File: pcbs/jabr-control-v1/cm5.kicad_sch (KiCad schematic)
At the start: 8 parts, among them SW201 SW_Push

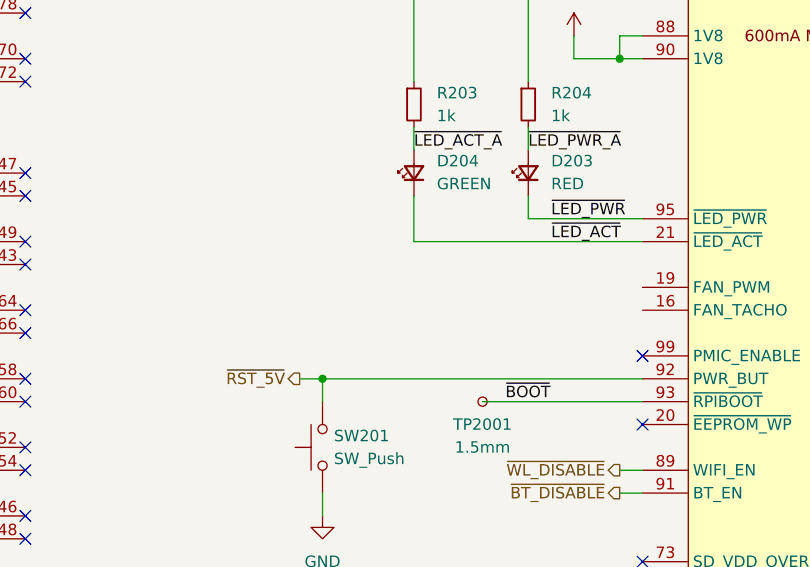
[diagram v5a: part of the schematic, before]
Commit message: Finished M.2 E-Key schematic
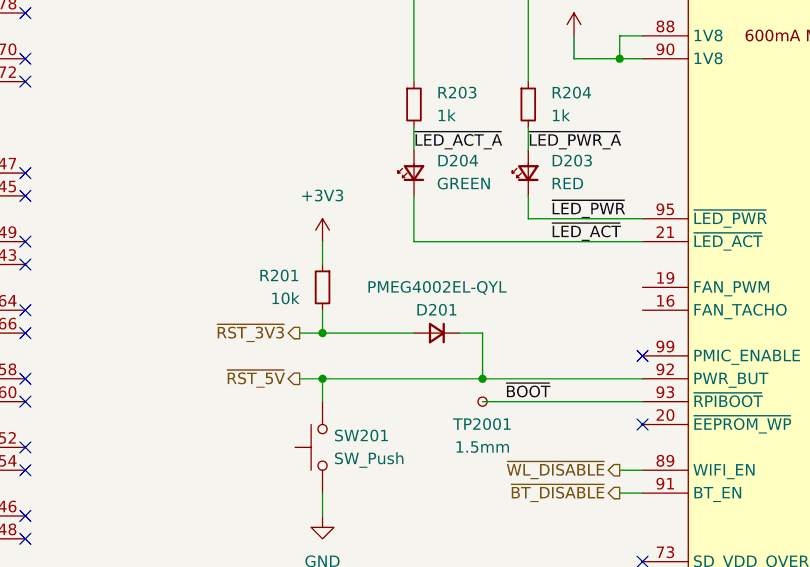
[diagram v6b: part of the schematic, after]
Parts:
- added D201: PMEG4002EL-QYL, project_footprints:PMEG4002EL-QYL, symbol DIODE:PMEG4002EL-QYL
- added R201: 10k, project_footprints:R_0402, symbol DEV:R_SMALL
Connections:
- net +3V3: now also R201.1
- net ~{RST_5V}: now also D201.1 (K)
- new net ~{RST_3V3}: D201.2 (A), R201.2

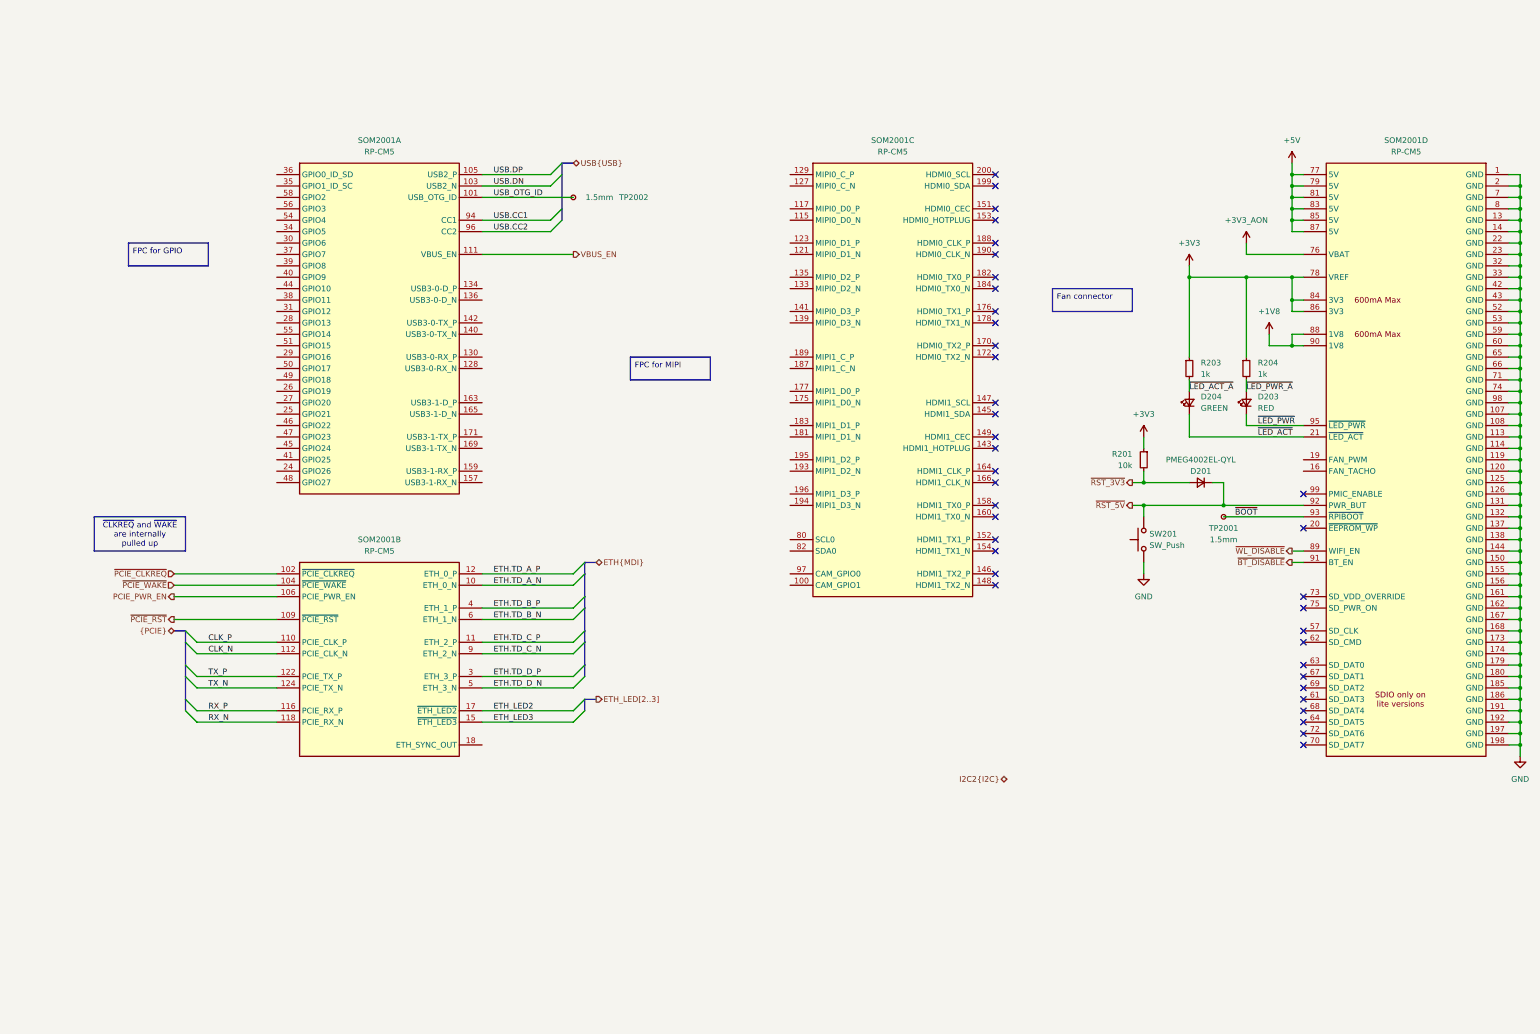
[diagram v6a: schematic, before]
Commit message: Schematic nearing completion, need to do GPIO and PHY decouplings caps
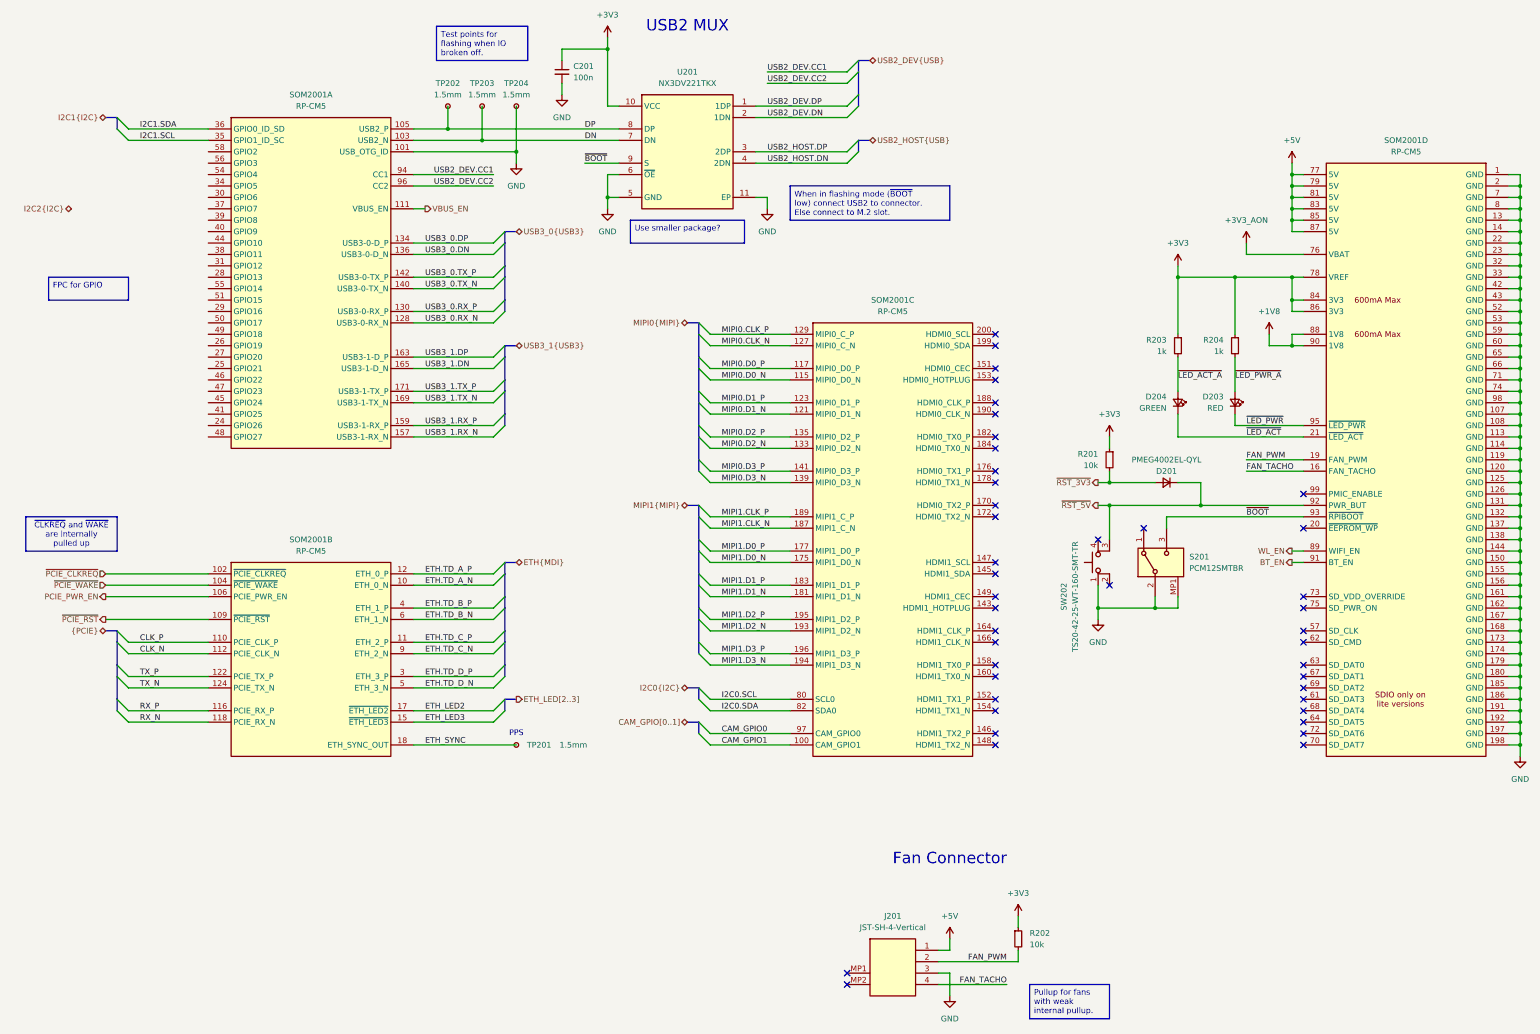
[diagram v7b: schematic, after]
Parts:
- removed SW201: SW_Push, symbol Switch:SW_Push
- removed TP2001, TP2002: 1.5mm, TestPoint:TestPoint_Pad_D1.5mm, symbol Connector:TestPoint_Small
- added C201: 100n, symbol DEV:C_SMALL
- added J201: JST-SH-4-Vertical, project_footprints:JST_SH_BM04B-SRSS-TB_1x04-1MP_P1.00mm_Vertical, symbol JST:JST-SH-4-Vertical
- added R202: 10k, project_footprints:R_0402, symbol DEV:R_SMALL
- added S201: PCM12SMTBR, project_footprints:PCM12SMTBR, symbol MECH:PCM12SMTBR
- added SW202: TS20-42-25-WT-160-SMT-TR, TS204225WT160SMTTR, symbol MECH:TS20-42-25-WT-160-SMT-TR
- added TP201, TP202, TP203, TP204: 1.5mm, project_footprints:TestPoint_Pad_D1.5mm, symbol Connector:TestPoint_Small
- added U201: NX3DV221TKX, project_footprints:SON50P300X300X100-11N, symbol COMM-MUX:NX3DV221TKX
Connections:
- net USB_OTG_ID is gone; now on net GND: SOM2001.101 (USB_OTG_ID)
- net +3V3: now also C201.1, R202.1, U201.10 (VCC)
- net +5V: now also J201.1
- net GND: now also C201.2, J201.3, S201.2 (COM), S201.MP1, S201.MP2, S201.MP3, S201.MP4, SW202.1, TP204.1, U201.11 (EP), U201.5 (GND), U201.6 (~{OE})
- net ~{BOOT}: now also S201.3 (NO), U201.9 (S)
- net ~{RST_5V}: now also SW202.3
- net ETH_SYNC: now reaches SOM2001.18 (ETH_SYNC_OUT)
- net ETH_SYNC: now also TP201.1
- net USB3_0.RX_N: now reaches SOM2001.128 (USB3-0-RX_N)
- net USB3_0.RX_P: now reaches SOM2001.130 (USB3-0-RX_P)
- net USB3_0.DP: now reaches SOM2001.134 (USB3-0-D_P)
- net USB3_0.DN: now reaches SOM2001.136 (USB3-0-D_N)
- net USB3_0.TX_N: now reaches SOM2001.140 (USB3-0-TX_N)
- net USB3_0.TX_P: now reaches SOM2001.142 (USB3-0-TX_P)
- net USB3_1.RX_N: now reaches SOM2001.157 (USB3-1-RX_N)
- net USB3_1.RX_P: now reaches SOM2001.159 (USB3-1-RX_P)
- net USB3_1.DP: now reaches SOM2001.163 (USB3-1-D_P)
- net USB3_1.DN: now reaches SOM2001.165 (USB3-1-D_N)
- net USB3_1.TX_N: now reaches SOM2001.169 (USB3-1-TX_N)
- net USB3_1.TX_P: now reaches SOM2001.171 (USB3-1-TX_P)
- net I2C1.SCL: now reaches SOM2001.35 (GPIO1_ID_SC)
- net I2C1.SDA: now reaches SOM2001.36 (GPIO0_ID_SD)
- net FAN_TACHO: now reaches SOM2001.16 (FAN_TACHO)
- net FAN_TACHO: now also J201.4
- net FAN_PWM: now reaches SOM2001.19 (FAN_PWM)
- net FAN_PWM: now also J201.2, R202.2
- net CAM_GPIO1: now reaches SOM2001.100 (CAM_GPIO1)
- net MIPI0.D0_N: now reaches SOM2001.115 (MIPI0_D0_N)
- net MIPI0.D0_P: now reaches SOM2001.117 (MIPI0_D0_P)
- net MIPI0.D1_N: now reaches SOM2001.121 (MIPI0_D1_N)
- net MIPI0.D1_P: now reaches SOM2001.123 (MIPI0_D1_P)
- net MIPI0.CLK_N: now reaches SOM2001.127 (MIPI0_C_N)
- net MIPI0.CLK_P: now reaches SOM2001.129 (MIPI0_C_P)
- net MIPI0.D2_N: now reaches SOM2001.133 (MIPI0_D2_N)
- net MIPI0.D2_P: now reaches SOM2001.135 (MIPI0_D2_P)
- net MIPI0.D3_N: now reaches SOM2001.139 (MIPI0_D3_N)
- net MIPI0.D3_P: now reaches SOM2001.141 (MIPI0_D3_P)
- net MIPI1.D0_N: now reaches SOM2001.175 (MIPI1_D0_N)
- net MIPI1.D0_P: now reaches SOM2001.177 (MIPI1_D0_P)
- net MIPI1.D1_N: now reaches SOM2001.181 (MIPI1_D1_N)
- net MIPI1.D1_P: now reaches SOM2001.183 (MIPI1_D1_P)
- net MIPI1.CLK_N: now reaches SOM2001.187 (MIPI1_C_N)
- net MIPI1.CLK_P: now reaches SOM2001.189 (MIPI1_C_P)
- net MIPI1.D2_N: now reaches SOM2001.193 (MIPI1_D2_N)
- net MIPI1.D3_N: now reaches SOM2001.194 (MIPI1_D3_N)
- net MIPI1.D2_P: now reaches SOM2001.195 (MIPI1_D2_P)
- net MIPI1.D3_P: now reaches SOM2001.196 (MIPI1_D3_P)
- net I2C0.SCL: now reaches SOM2001.80 (SCL0)
- net I2C0.SDA: now reaches SOM2001.82 (SDA0)
- net CAM_GPIO0: now reaches SOM2001.97 (CAM_GPIO0)
- net USB.CC1 renamed USB2_DEV.CC1
- net USB.CC2 renamed USB2_DEV.CC2
- net USB.DN renamed DN
- net DN: now also TP203.1, U201.7 (DN)
- net USB.DP renamed DP
- net DP: now also TP202.1, U201.8 (DP)
- net ~{BT_DISABLE} renamed BT_EN
- net ~{WL_DISABLE} renamed WL_EN
- new net USB2_DEV.DN: U201.2 (1DN)
- new net USB2_DEV.DP: U201.1 (1DP)
- new net USB2_HOST.DN: U201.4 (2DN)
- new net USB2_HOST.DP: U201.3 (2DP)
- no-connect marks 38 -> 43
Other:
- note added: "Fan Connector"
- note added: "PPS"
- note added: "USB2 MUX"
- moved on the sheet: D201, D203, D204, R201, R203, R204, SOM2001A, SOM2001B, SOM2001C
